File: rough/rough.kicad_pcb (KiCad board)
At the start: 2 copper layers, 127 x 127 mm, 3 parts

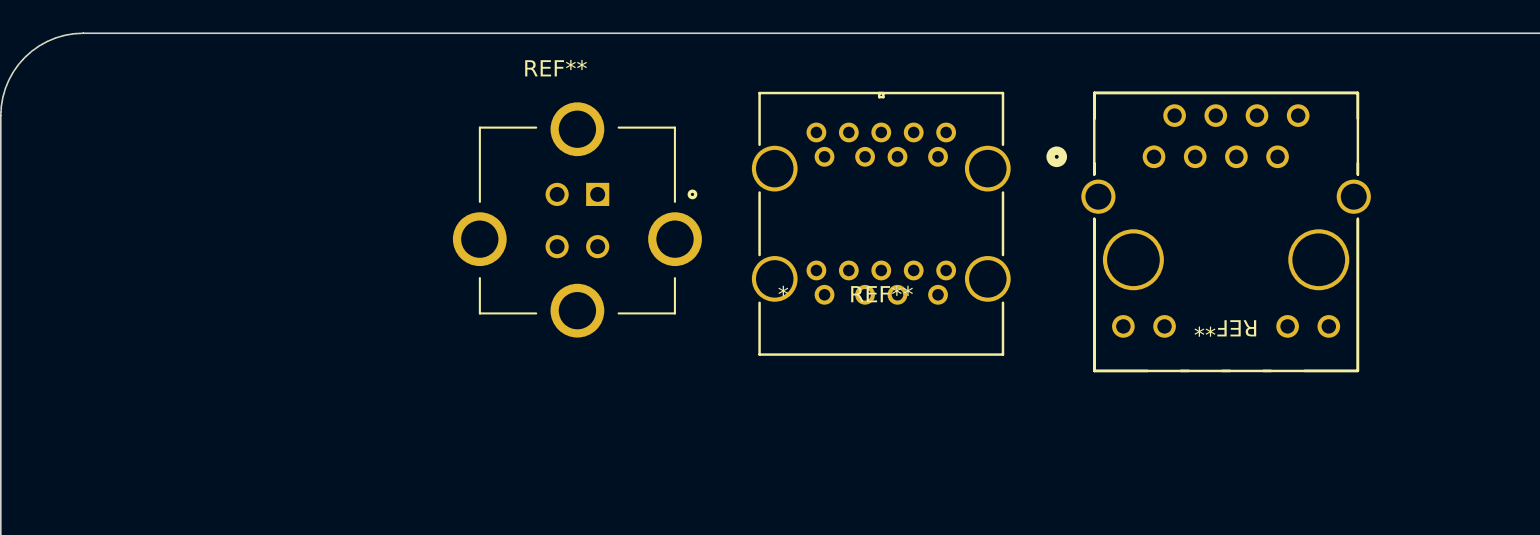
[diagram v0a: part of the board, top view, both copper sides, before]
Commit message: Add footprints and symbols for components we plan to use
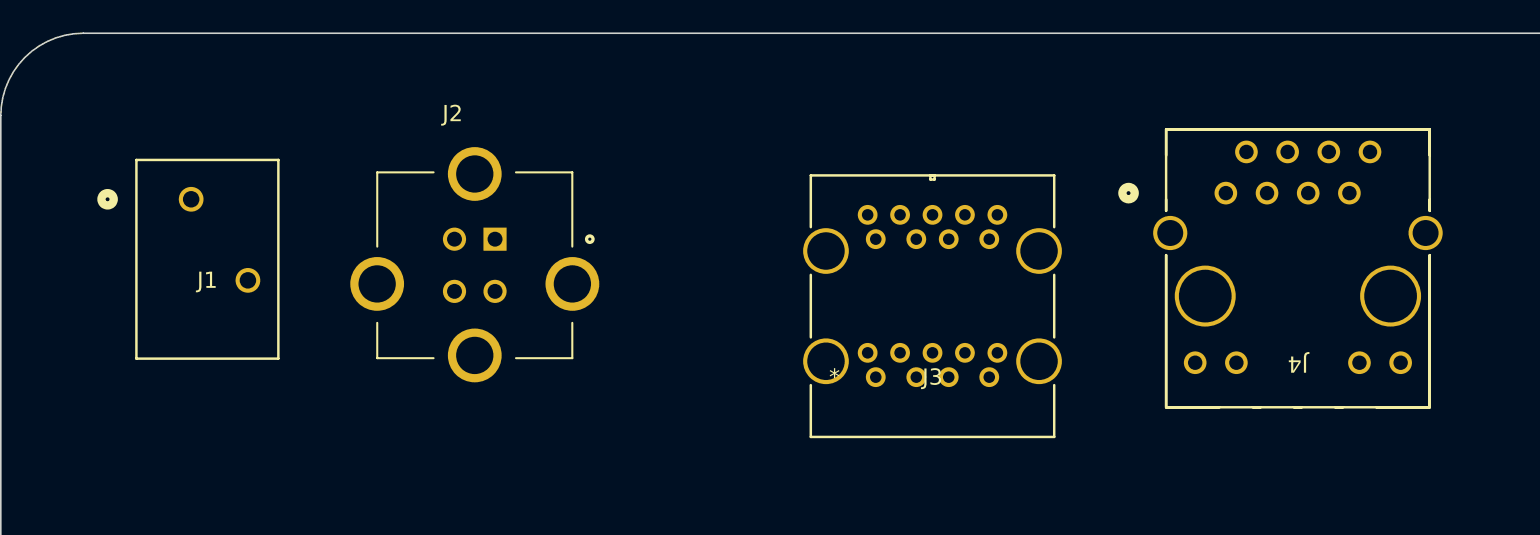
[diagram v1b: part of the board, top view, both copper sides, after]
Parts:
- removed REF**: TE_5788336-1, SnapEDA:TE_5788336-1
- removed REF**: CONN12_0012BENL_TAL, SnapEDA:CONN12_0012BENL_TAL
- removed REF**: 48409-0003_MOL, SnapEDA:48409-0003_MOL
- added J1: 250-202 Wago, SnapEDA:CONN_250-202_WAG, F.Cu at (62.5, 35.6)
- added J2: 5788336-1 TE USB-B, SnapEDA:TE_5788336-1, F.Cu at (80.0, 40.9)
- added J3: 484090003 Molex 2x USB-A v3, SnapEDA:48409-0003_MOL, F.Cu at (104.8, 46.6)
- added J4: TMJD0012BENL Tagolas Ethernet, SnapEDA:CONN12_0012BENL_TAL, F.Cu at (126.3, 35.3)

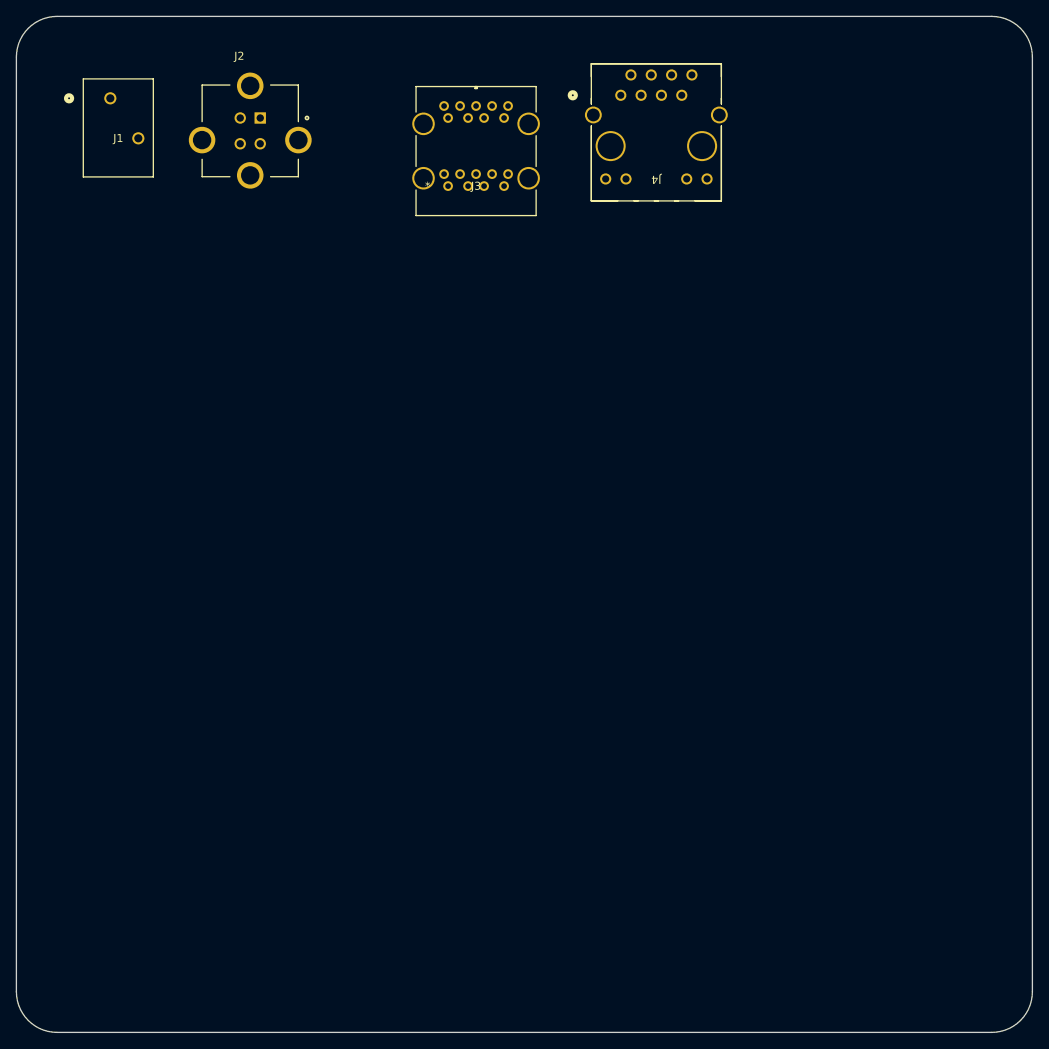
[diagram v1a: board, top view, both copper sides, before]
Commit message: Break libs by MFG
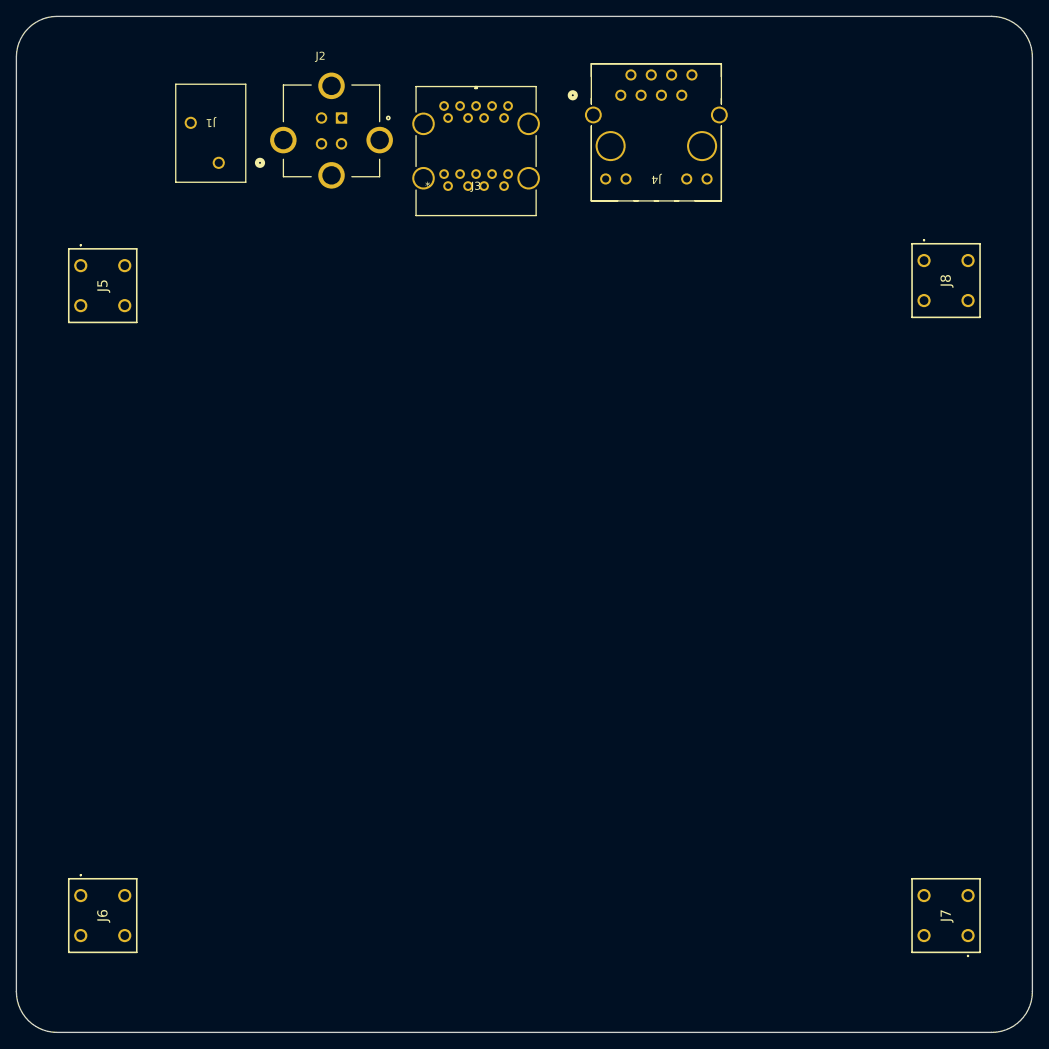
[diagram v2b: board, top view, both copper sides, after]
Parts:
- added J5: 1825960000 Weidmuller 2pos wide, Weidmuller:CONN_1825960000 2pos Wide, F.Cu at (58.8, 56.6)
- added J6: 1825960000 Weidmuller 2pos wide, Weidmuller:CONN_1825960000 2pos Wide, F.Cu at (58.8, 135.3)
- added J7: 1825960000 Weidmuller 2pos wide, Weidmuller:CONN_1825960000 2pos Wide, F.Cu at (169.8, 140.3)
- added J8: 1825960000 Weidmuller 2pos wide, Weidmuller:CONN_1825960000 2pos Wide, F.Cu at (164.3, 55.9)
- J1: footprint SnapEDA:CONN_250-202_WAG -> Wago:CONN_250-202
- J2: footprint SnapEDA:TE_5788336-1 -> TE:TE_5788336-1_USB-B
- J3: footprint SnapEDA:48409-0003_MOL -> Molex:48409-0003_MOL
- J4: footprint SnapEDA:CONN12_0012BENL_TAL -> Taoglas:CONN12_0012BENL_TAL
- moved J1 15.8 mm to (76.1, 43.7), turned to 180 degrees
- moved J2 10.2 mm to (90.2, 40.9)

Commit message: Playing with weidmuller
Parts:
- added J10: 1826000000 6pos wide, Weidmuller:1826000000, F.Cu at (69.8, 69.9)
- added J11: 1826000000 6pos wide, Weidmuller:1826000000, F.Cu at (80.9, 70.1)
- added J12: 1825970000 3pos wide, Weidmuller:1825970000, F.Cu at (159.4, 74.4)
- added J13: 1825970000 3pos wide, Weidmuller:1825970000, F.Cu at (159.4, 85.0)
- added J14: 1825970000 3pos wide, Weidmuller:1825970000, F.Cu at (159.4, 95.5)
- added J15: 1825970000 3pos wide, Weidmuller:1825970000, F.Cu at (159.4, 106.2)
- added J16: 1825970000 3pos wide, Weidmuller:1825970000, F.Cu at (159.4, 116.7)
- added J17: 1825970000 3pos wide, Weidmuller:1825970000, F.Cu at (159.4, 127.3)
- added J9: 1826000000 6pos wide, Weidmuller:1826000000, F.Cu at (59.1, 70.0)
- J5, J6, J7, J8: footprint Weidmuller:CONN_1825960000 2pos Wide -> Weidmuller:1825960000

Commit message: wip
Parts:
- moved J7 25.6 mm to (145.2, 133.1)
- moved J6 19.0 mm to (62.3, 116.6)
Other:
- outline, holes or cut-outs redrawn
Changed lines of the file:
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@@
   )
   (footprint "Weidmuller:1825960000" (layer "F.Cu")
-    (at 169.755 140.295 90)
+    (at 145.244 133.056 90)
     (descr "Printed circuit board terminals, 5.00 mm, Number of poles: 2, 180°, Solder pin length: 3.5 mm, black, PUSH IN with actuator, Clamping range, max. [rated connection]: 1.5 mm², Tube")
     (tags "Connector")
@@
   )
   (footprint "Weidmuller:1825960000" (layer "F.Cu")
-    (at 58.845 135.295 -90)
+    (at 62.274 116.626 -90)
     (descr "Printed circuit board terminals, 5.00 mm, Number of poles: 2, 180°, Solder pin length: 3.5 mm, black, PUSH IN with actuator, Clamping range, max. [rated connection]: 1.5 mm², Tube")
     (tags "Connector")
@@
   (gr_line (start 55.88 25.4) (end 172.72 25.4)
     (stroke (width 0.1) (type default)) (layer "Edge.Cuts"))
+  (gr_circle (center 61.214 142.24) (end 66.294 142.24)
+    (stroke (width 0.1) (type default)) (fill none) (layer "Edge.Cuts"))
   (gr_arc (start 172.72 25.4) (mid 176.312102 26.887898) (end 177.8 30.48)
     (stroke (width 0.1) (type default)) (layer "Edge.Cuts"))
   (gr_line (start 50.8 147.32) (end 50.8 30.48)
     (stroke (width 0.1) (type default)) (layer "Edge.Cuts"))
+  (gr_circle (center 60.96 35.56) (end 66.04 35.56)
+    (stroke (width 0.1) (type default)) (fill none) (layer "Edge.Cuts"))
+  (gr_circle (center 167.64 35.56) (end 172.72 35.56)
+    (stroke (width 0.1) (type default)) (fill none) (layer "Edge.Cuts"))
   (gr_arc (start 177.8 147.32) (mid 176.312102 150.912102) (end 172.72 152.4)
     (stroke (width 0.1) (type default)) (layer "Edge.Cuts"))
@@
   (gr_line (start 177.8 30.48) (end 177.8 147.32)
     (stroke (width 0.1) (type default)) (layer "Edge.Cuts"))
+  (gr_circle (center 167.64 142.24) (end 172.72 142.24)
+    (stroke (width 0.1) (type default)) (fill none) (layer "Edge.Cuts"))
 )
